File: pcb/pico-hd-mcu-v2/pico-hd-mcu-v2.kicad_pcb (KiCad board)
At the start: 2 copper layers, 80 x 54 mm, 34 parts

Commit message: pcb update
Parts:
- removed the REF** at (58.4, 67.7)
- removed the REF** at (34.2, 57.3)
- moved ? 2.13 mm to (21.7, 47.5)
- moved ? 1.71 mm to (21.6, 31.6)
- moved ? 1.12 mm to (21.6, 64.8)
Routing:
- net GND: track 206.0 -> 203.6 mm
- net SIG_L_OUT: track 9.87 -> 9.08 mm
- net SIG_R_IN: track 20.1 -> 20.8 mm

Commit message: pcb update
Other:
- board size 80 x 54 mm -> 81 x 56 mm

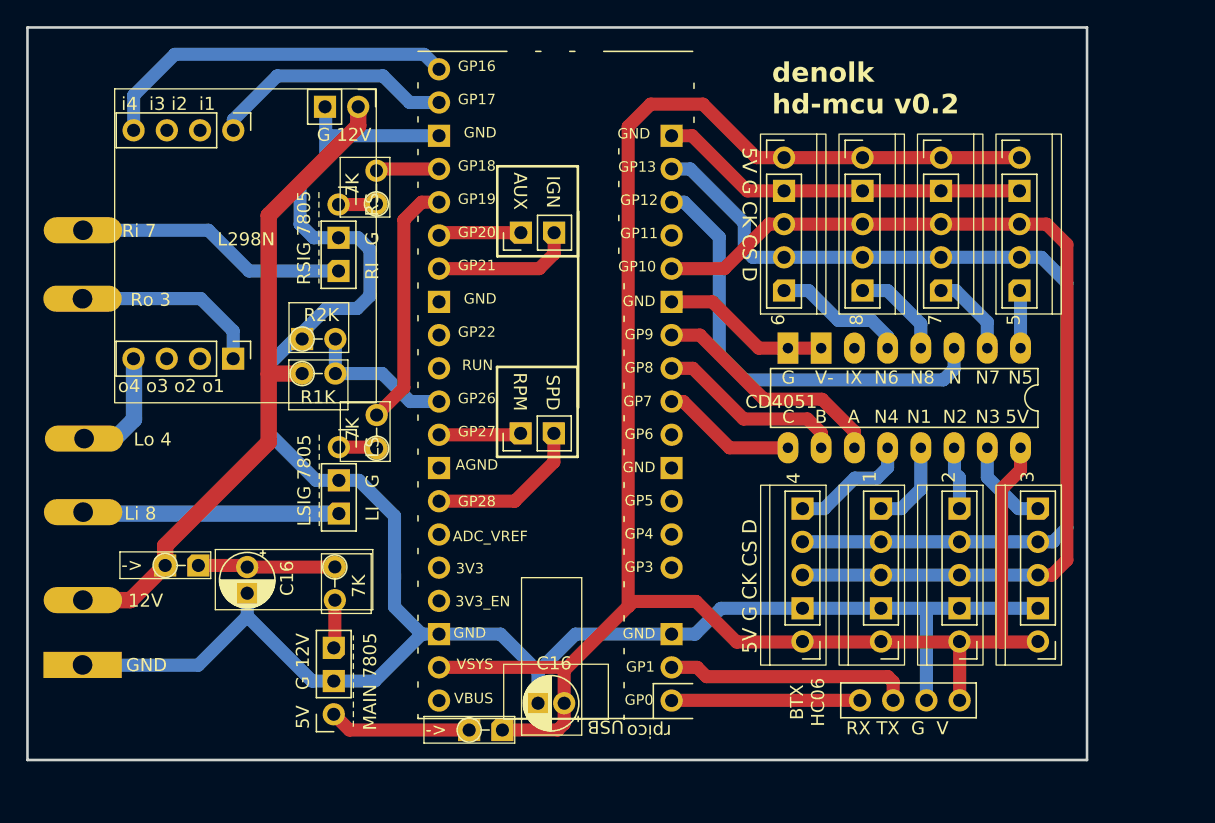
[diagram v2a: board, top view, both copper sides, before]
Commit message: added 12v5 power supply submodule
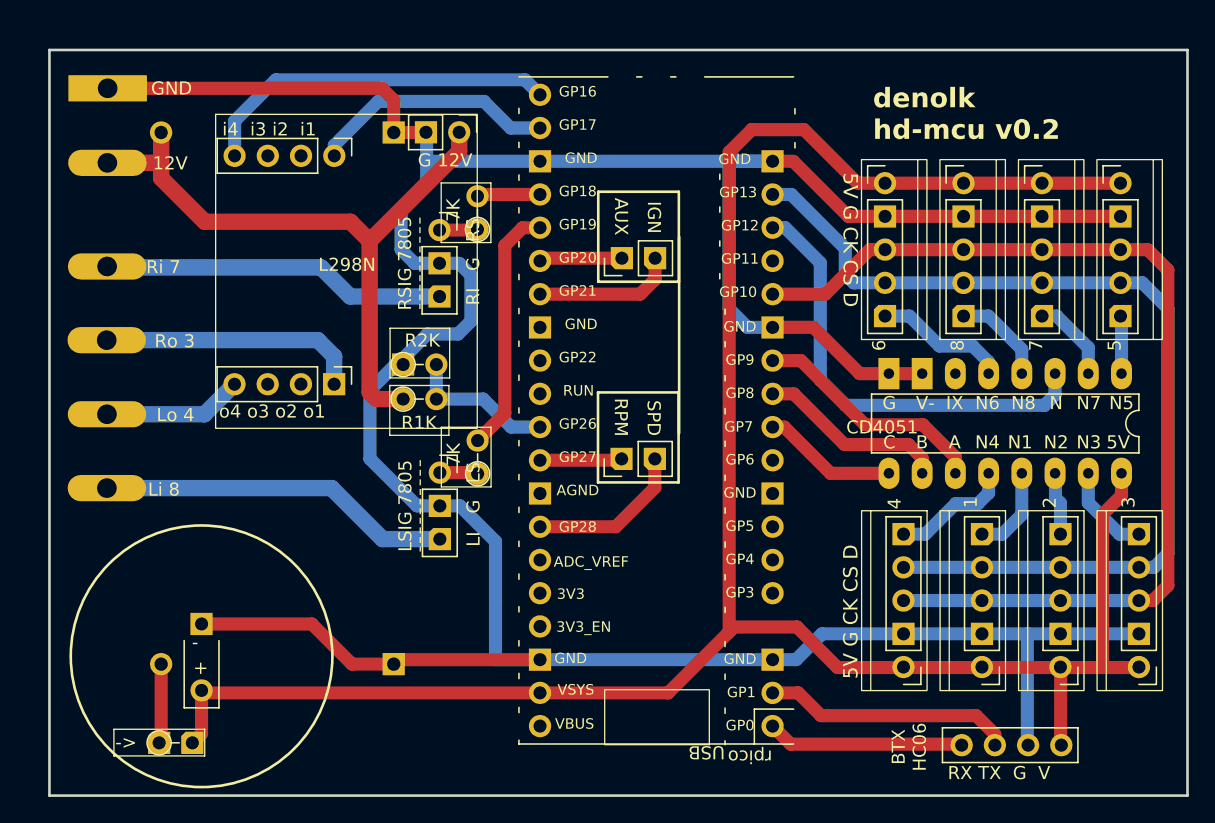
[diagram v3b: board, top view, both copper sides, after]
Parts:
- removed the -> at (27.9, 57.2)
- removed the 7K at (40.9, 57.3)
- removed MAIN 7805: PinSocket_1x03_P2.54mm_Vertical, Connector_PinSocket_2.54mm:PinSocket_1x03_P2.54mm_Vertical
- removed the REF** at (58.4, 67.7)
- removed the REF** at (34.2, 57.3)
- added REF**: capacitor_5v5_bat_20mm, denolk:capacitor_5v5_bat_20mm, F.Cu at (30.7, 63.9)
- added REF**: switch_regulator_12v5v, denolk:switch_regulator_12v5v, B.Cu at (36.5, 48.9)
- moved ? 44.1 mm to (23.5, 20.7)
- moved ? 33.5 mm to (23.5, 26.4)
- moved -> 23.7 mm to (27.4, 70.7)
- moved ? 8.50 mm to (87.3, 72.2)
- moved REF** 7.96 mm to (65.5, 44.7)
- moved 7K 7.96 mm to (51.8, 50.2)
- moved CD4051 7.96 mm to (101.0, 42.6)
- moved LSIG 7805 7.96 mm to (48.9, 50.1)
- moved R1K 7.96 mm to (46.1, 44.5)
- moved R2K 7.96 mm to (46.1, 41.8)
- moved REF** 7.96 mm to (41.8, 33.2)
- moved REF** 7.96 mm to (62.8, 49.0)
- moved RSIG 7805 7.96 mm to (48.9, 31.5)
- moved 1 7.96 mm to (90.3, 64.9)
- moved 2 7.96 mm to (96.3, 64.9)
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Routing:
- net GND: track 203.6 -> 260.1 mm
- net 5V: track 158.7 -> 176.0 mm
- net 12V: track 65.9 -> 51.6 mm
- net SIG_L_IN: track 19.4 -> 27.1 mm
- net SIG_R_IN: track 20.8 -> 26.4 mm
- net SIG_R_OUT: track 14.7 -> 20.0 mm
- net SIG_L_OUT: track 9.08 -> 10.8 mm
- net D_BT_TX: track 14.4 -> 15.1 mm
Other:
- board size 81 x 56 mm -> 87 x 57 mm
